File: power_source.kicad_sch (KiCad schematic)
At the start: 19 parts, among them J2 USB_B_Micro, Q1 Q_PMOS_GDS, Q2 BSS138, SW2 SW_SPDT

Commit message: make board
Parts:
- removed BT1: BackupBatt, symbol Device:Battery_Cell
- removed C5, C6: C, symbol Device:C
- removed D1: D_Schottky, symbol Device:D_Schottky
- removed D2: D, symbol Device:D
- removed J2: USB_B_Micro, symbol Connector:USB_B_Micro
- removed L1: L, symbol Device:L
- removed Q1: Q_PMOS_GDS, symbol Device:Q_PMOS_GDS
- removed Q2: BSS138, Package_TO_SOT_SMD:SOT-23, symbol Transistor_FET:BSS138
- removed R24: 10k, symbol Device:R
- removed R25: 100k, symbol Device:R
- removed R26, R27: R, symbol Device:R
- removed U7: ~, symbol balloon_lib:NJW1616F1-AT
- added C17 (x2): 4.7u, Capacitor_SMD:C_0603_1608Metric_Pad1.08x0.95mm_HandSolder, symbol Device:C
- added C4 (x3): 100n, Capacitor_SMD:C_0603_1608Metric_Pad1.08x0.95mm_HandSolder, symbol Device:C
- added D3, D4: OSG50603C1E, LED_SMD:LED_0603_1608Metric_Pad1.05x0.95mm_HandSolder, symbol Device:LED
- added D5: RS1M, Diode_SMD:D_SMA_Handsoldering, symbol Device:D
- added Q1, Q3: BSS138, Package_TO_SOT_SMD:SOT-23, symbol Transistor_FET:BSS138
- added Q2: 2SJ681, Package_TO_SOT_THT:SIPAK_Vertical, symbol Device:Q_PMOS_GDS
- added R29: 100, Resistor_SMD:R_0603_1608Metric_Pad0.98x0.95mm_HandSolder, symbol Device:R
- added R30: 10k, Resistor_SMD:R_0603_1608Metric_Pad0.98x0.95mm_HandSolder, symbol Device:R
- added R31, R32: 2.2k, Resistor_SMD:R_0603_1608Metric_Pad0.98x0.95mm_HandSolder, symbol Device:R
- added U10, U9: TCK107AF, Package_TO_SOT_SMD:SOT-23-5_HandSoldering, symbol balloon_lib:TCK107
- added U7: M78AR033-1, Package_TO_SOT_THT:TO-220-3_Vertical, symbol Regulator_Linear:LM7805_TO220
- added U8: MCP3425A0T-ECH, Package_TO_SOT_SMD:SOT-23-6_Handsoldering, symbol Analog_ADC:MCP3425A0T-ECH
- BT2, BT3, BT4: footprint (none) -> balloon:CR123A
- R28: footprint (none) -> Resistor_SMD:R_0603_1608Metric_Pad0.98x0.95mm_HandSolder
- SW2: footprint (none) -> Connector_PinSocket_2.54mm:PinSocket_1x03_P2.54mm_Vertical
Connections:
- net +3V3: now also C17.1, C17.1, C4.1, C4.1, C4.1, U10.5 (VIN), U7.3 (VO), U8.5 (Vdd), U9.5 (VIN)
- net GND1: now also C17.2, C17.2, C4.2, C4.2, C4.2, Q1.2 (S), Q3.2 (S), R31.2, R32.2, U10.2 (GND), U7.2 (GND), U8.2 (Vss), U8.6 (Vin-), U9.2 (GND)
- net at R28.1: now also BT2.1 (+), Q2.3 (S), R30.1; no longer SW2.3 (C)
- net at R28.2: now also Q1.3 (D), Q3.1 (G)
- net at SW2.2 (B): now also D3.2 (A), D5.1 (K), Q2.2 (D)
- new net: D4.1 (K), R32.1
- new net: Q2.1 (G), Q3.3 (D), R30.2
- new net: D3.1 (K), R31.1
- new net: Q1.1 (G), R29.2
- new net 5VIN: D4.2 (A), D5.2 (A), R29.1
- new net CTRL_COMM: U10.3 (CTRL)
- new net CTRL_SENSE: U9.3 (CTRL)
- new net SCL: U8.3 (SCL)
- new net SDA: U8.4 (SDA)
- new net VCOMM: U10.1 (VOUT)
- new net VIN: SW2.3 (C), U7.1 (VI), U8.1 (Vin+)
- new net VSENSE: U9.1 (VOUT)
- no-connect marks 4 -> 1
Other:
- moved on the sheet: BT2, BT3, BT4

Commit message: replace PCB
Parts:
- added J8: Bypass, Connector_PinSocket_2.54mm:PinSocket_1x02_P2.54mm_Vertical, symbol Connector:Conn_01x02_Pin
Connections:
- net GND1: now also J8.2 (Pin_2)
- net at BT3.2 (-), BT4.1 (+): now also J8.1 (Pin_1)
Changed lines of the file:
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@@
   (junction (at 151.13 76.2) (diameter 0) (color 0 0 0 0)
   )
+  (junction (at 58.42 107.95) (diameter 0) (color 0 0 0 0)
+  )
   (junction (at 176.53 83.82) (diameter 0) (color 0 0 0 0)
+  )
+  (junction (at 58.42 100.33) (diameter 0) (color 0 0 0 0)
   )
   (junction (at 73.66 80.01) (diameter 0) (color 0 0 0 0)
@@
     (stroke (width 0) (type default))
   )
+  (wire (pts (xy 44.45 104.14) (xy 49.53 104.14))
+    (stroke (width 0) (type default))
+  )
   (wire (pts (xy 165.1 134.62) (xy 171.45 134.62))
     (stroke (width 0) (type default))
@@
     (stroke (width 0) (type default))
   )
+  (wire (pts (xy 44.45 106.68) (xy 44.45 107.95))
+    (stroke (width 0) (type default))
+  )
   (wire (pts (xy 71.12 111.76) (xy 71.12 128.27))
     (stroke (width 0) (type default))
@@
     (stroke (width 0) (type default))
   )
+  (wire (pts (xy 44.45 107.95) (xy 58.42 107.95))
+    (stroke (width 0) (type default))
+  )
   (wire (pts (xy 93.98 87.63) (xy 99.06 87.63))
     (stroke (width 0) (type default))
@@
     (stroke (width 0) (type default))
   )
+  (wire (pts (xy 49.53 104.14) (xy 49.53 100.33))
+    (stroke (width 0) (type default))
+  )
   (wire (pts (xy 62.23 80.01) (xy 58.42 80.01))
+    (stroke (width 0) (type default))
+  )
+  (wire (pts (xy 49.53 100.33) (xy 58.42 100.33))
     (stroke (width 0) (type default))
   )
@@
         )
       )
+    )
+  )
+  (symbol (lib_id "Connector:Conn_01x02_Pin") (at 39.37 104.14 0) (unit 1)
+    (in_bom yes) (on_board yes) (dnp no) (fields_autoplaced)
+    (property "Reference" "J8" (at 40.005 99.9195 0)
+      (effects (font (size 1.27 1.27)))
+    )
+    (property "Value" "Bypass" (at 40.005 102.3437 0)
+      (effects (font (size 1.27 1.27)))
+    )
+    (property "Footprint" "Connector_PinSocket_2.54mm:PinSocket_1x02_P2.54mm_Vertical" (at 39.37 104.14 0)
+      (effects (font (size 1.27 1.27)) hide)
+    )
+    (property "Datasheet" "~" (at 39.37 104.14 0)
+      (effects (font (size 1.27 1.27)) hide)
+    )
+    (pin "2")
+    (pin "1")
+    (instances
+      (project "balloon"
+        (path "/390c33b5-3f3b-4c86-a202-e8d785058178/a8964fff-36f8-4d65-a455-a6f79e0406e2"
+          (reference "J8") (unit 1)
+        )
+      )

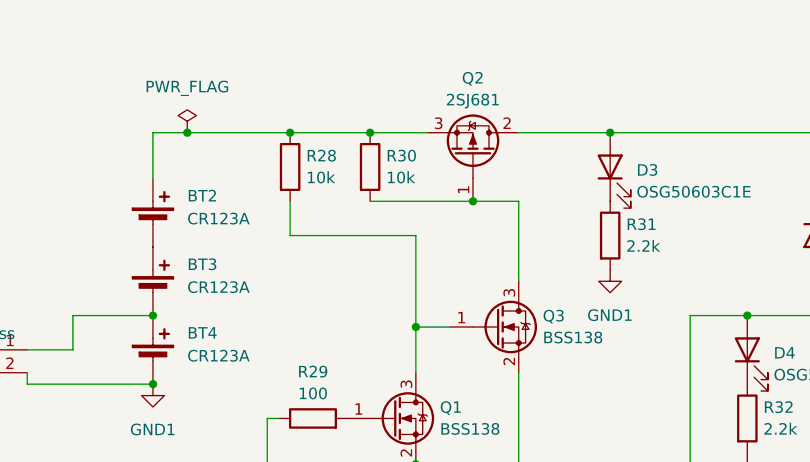
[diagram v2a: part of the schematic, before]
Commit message: add stmcube
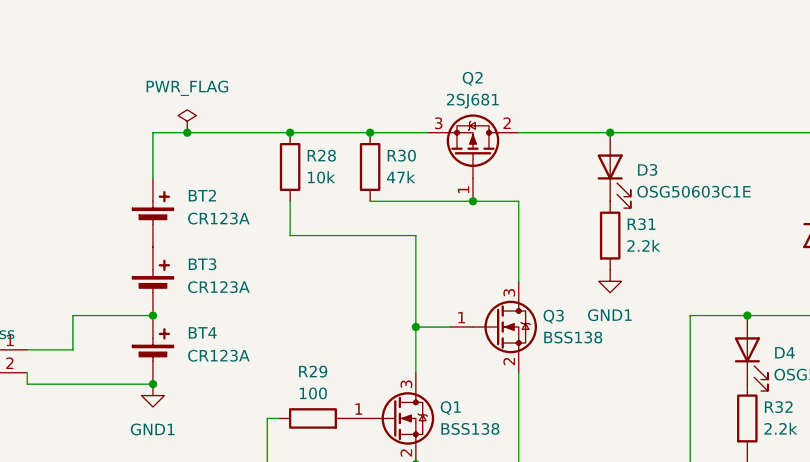
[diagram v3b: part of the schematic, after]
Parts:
- R30: value 10k -> 47k
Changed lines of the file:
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@@
       (effects (font (size 1.27 1.27)) hide)
     )
-    (pin "2")
-    (pin "1")
+    (pin "1")
+    (pin "2")
     (instances
       (project "balloon"
@@
       (effects (font (size 1.27 1.27)) hide)
     )
+    (pin "1")
+    (pin "2")
+    (pin "3")
+    (pin "4")
     (pin "5")
-    (pin "4")
-    (pin "1")
-    (pin "3")
-    (pin "2")
     (pin "6")
     (instances
@@
       (effects (font (size 1.27 1.27)) hide)
     )
-    (pin "2")
-    (pin "1")
+    (pin "1")
+    (pin "2")
     (pin "3")
     (instances
@@
       (effects (font (size 1.27 1.27)) hide)
     )
-    (pin "2")
-    (pin "1")
+    (pin "1")
+    (pin "2")
     (instances
       (project "balloon"
@@
       (effects (font (size 1.27 1.27)) hide)
     )
+    (pin "1")
     (pin "2")
     (pin "3")
-    (pin "1")
+    (pin "4")
     (pin "5")
-    (pin "4")
     (instances
       (project "balloon"
@@
       (effects (font (size 1.27 1.27)) hide)
     )
+    (pin "1")
+    (pin "2")
     (pin "3")
-    (pin "2")
-    (pin "1")
     (instances
       (project "balloon"
@@
       (effects (font (size 1.27 1.27)) (justify left))
     )
-    (property "Value" "10k" (at 84.328 85.0321 0)
+    (property "Value" "47k" (at 84.328 85.0321 0)
       (effects (font (size 1.27 1.27)) (justify left))
     )
@@
       (effects (font (size 1.27 1.27)) hide)
     )
+    (pin "1")
     (pin "2")
     (pin "3")
-    (pin "1")
+    (pin "4")
     (pin "5")
-    (pin "4")
-    (instances
-      (project "balloon"
+    (instances
+      (project "balloon"

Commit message: set gerber
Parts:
- U10, U9: Price (none) -> 30
- U7: Price (none) -> 500
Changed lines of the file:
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@@
+      (effects (font (size 1.27 1.27)) hide)
+    )
+    (property "Price" "" (at 124.46 111.76 0)
       (effects (font (size 1.27 1.27)) hide)
     )
@@
       (effects (font (size 1.27 1.27)) hide)
     )
+    (property "Price" "" (at 190.5 80.01 0)
+      (effects (font (size 1.27 1.27)) hide)
+    )
     (pin "1")
     (pin "2")
@@
       (effects (font (size 1.27 1.27)) (justify left) hide)
     )
+    (property "Price" "" (at 96.52 101.6 0)
+      (effects (font (size 1.27 1.27)) hide)
+    )
     (pin "1")
     (pin "2")
@@
     )
     (property "Datasheet" "~" (at 109.22 91.44 0)
+      (effects (font (size 1.27 1.27)) hide)
+    )
+    (property "Price" "" (at 109.22 91.44 0)
       (effects (font (size 1.27 1.27)) hide)
     )
@@
       (effects (font (size 1.27 1.27)) hide)
     )
+    (property "Price" "" (at 219.71 107.95 0)
+      (effects (font (size 1.27 1.27)) hide)
+    )
     (pin "1")
     (pin "2")
@@
       (effects (font (size 1.27 1.27)) hide)
     )
+    (property "Price" "" (at 73.66 83.82 0)
+      (effects (font (size 1.27 1.27)) hide)
+    )
     (pin "1")
     (pin "2")
@@
     )
     (property "Datasheet" "~" (at 58.42 103.886 90)
+      (effects (font (size 1.27 1.27)) hide)
+    )
+    (property "Price" "" (at 58.42 105.41 0)
       (effects (font (size 1.27 1.27)) hide)
     )
@@
       (effects (font (size 1.27 1.27)) hide)
     )
+    (property "Price" "" (at 201.93 80.01 0)
+      (effects (font (size 1.27 1.27)) hide)
+    )
     (pin "1")
     (pin "2")
@@
     )
     (property "Datasheet" "http://ww1.microchip.com/downloads/en/DeviceDoc/22072b.pdf" (at 184.15 132.08 0)
+      (effects (font (size 1.27 1.27)) hide)
+    )
+    (property "Price" "" (at 184.15 132.08 0)
       (effects (font (size 1.27 1.27)) hide)
     )
@@
       (effects (font (size 1.27 1.27)) hide)
     )
+    (property "Price" "" (at 109.22 83.82 0)
+      (effects (font (size 1.27 1.27)) hide)
+    )
     (pin "1")
     (pin "2")
@@
       (effects (font (size 1.27 1.27)) hide)
     )
+    (property "Price" "500" (at 176.53 76.2 0)
+      (effects (font (size 1.27 1.27)) hide)
+    )
     (pin "1")
     (pin "2")
@@
       (effects (font (size 1.27 1.27)) hide)
     )
+    (property "Price" "" (at 58.42 90.17 0)
+      (effects (font (size 1.27 1.27)) hide)
+    )
     (pin "1")
     (pin "2")
@@
       (effects (font (size 1.27 1.27)) hide)
     )
+    (property "Price" "" (at 39.37 104.14 0)
+      (effects (font (size 1.27 1.27)) hide)
+    )
     (pin "1")
     (pin "2")
@@
       (effects (font (size 1.27 1.27)) hide)
     )
+    (property "Price" "" (at 199.39 144.78 0)
+      (effects (font (size 1.27 1.27)) hide)
+    )
     (pin "1")
     (pin "2")
@@
     )
     (property "Datasheet" "~" (at 76.2 111.76 0)
+      (effects (font (size 1.27 1.27)) hide)
+    )
+    (property "Price" "" (at 76.2 111.76 0)
       (effects (font (size 1.27 1.27)) hide)
     )
@@
       (effects (font (size 1.27 1.27)) hide)
     )
+    (property "Price" "30" (at 250.19 125.73 0)
+      (effects (font (size 1.27 1.27)) hide)
+    )
     (pin "1")
     (pin "2")
@@
       (effects (font (size 1.27 1.27)) hide)
     )
+    (property "Price" "" (at 132.08 91.44 0)
+      (effects (font (size 1.27 1.27)) hide)
+    )
     (pin "1")
     (pin "2")
@@
       (effects (font (size 1.27 1.27)) hide)
     )
+    (property "Price" "" (at 124.46 104.14 0)
+      (effects (font (size 1.27 1.27)) hide)
+    )
     (pin "1")
     (pin "2")
@@
     )
     (property "Datasheet" "~" (at 58.42 96.266 90)
+      (effects (font (size 1.27 1.27)) hide)
+    )
+    (property "Price" "" (at 58.42 97.79 0)
       (effects (font (size 1.27 1.27)) hide)
     )
@@
       (effects (font (size 1.27 1.27)) hide)
     )
+    (property "Price" "" (at 93.98 82.55 0)
+      (effects (font (size 1.27 1.27)) hide)
+    )
     (pin "1")
     (pin "2")
@@
     (property "Datasheet" "https://www.onsemi.com/pub/Collateral/BSS138-D.PDF" (at 85.09 111.76 0)
       (effects (font (size 1.27 1.27)) (justify left) hide)
+    )
+    (property "Price" "" (at 85.09 111.76 0)
+      (effects (font (size 1.27 1.27)) hide)
     )
     (pin "1")
@@
       (effects (font (size 1.27 1.27)) hide)
     )
+    (property "Price" "" (at 219.71 128.27 0)
+      (effects (font (size 1.27 1.27)) hide)
+    )
     (pin "1")
     (pin "2")
@@
     )
     (property "Datasheet" "~" (at 82.55 83.82 0)
+      (effects (font (size 1.27 1.27)) hide)
+    )
+    (property "Price" "" (at 82.55 83.82 0)
       (effects (font (size 1.27 1.27)) hide)
     )
@@
       (effects (font (size 1.27 1.27)) hide)
     )
+    (property "Price" "30" (at 250.19 109.22 0)
+      (effects (font (size 1.27 1.27)) hide)
+    )
     (pin "1")
     (pin "2")
@@
       (effects (font (size 1.27 1.27)) hide)
     )
+    (property "Price" "" (at 139.7 76.2 0)
+      (effects (font (size 1.27 1.27)) hide)
+    )

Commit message: change pow
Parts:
- removed D3, D4: OSG50603C1E, LED_SMD:LED_0603_1608Metric_Pad1.05x0.95mm_HandSolder, symbol Device:LED
- removed D5: RS1M, Diode_SMD:D_SMA_Handsoldering, symbol Device:D
- removed Q1, Q3: BSS138, Package_TO_SOT_SMD:SOT-23, symbol Transistor_FET:BSS138
- removed Q2: 2SJ681, Package_TO_SOT_THT:SIPAK_Vertical, symbol Device:Q_PMOS_GDS
- added Q1, Q2: Si9933ADY, symbol Device:Q_Dual_PMOS_S1G1S2G2D2D2D1D1
- added R37, R38, R39, R40, R41, R42: R, symbol Device:R
- added SW3: SW_SPDT, Connector_PinSocket_2.54mm:PinSocket_1x03_P2.54mm_Vertical, symbol Switch:SW_SPDT
- added U2: LTC4417CGN, Package_SO:SSOP-24_3.9x8.7mm_P0.635mm, symbol Power_Management:LTC4417CGN
- R28: value 10k -> R; footprint Resistor_SMD:R_0603_1608Metric_Pad0.98x0.95mm_HandSolder -> (none)
- R29: value 100 -> R; footprint Resistor_SMD:R_0603_1608Metric_Pad0.98x0.95mm_HandSolder -> (none)
- R30: value 47k -> R; footprint Resistor_SMD:R_0603_1608Metric_Pad0.98x0.95mm_HandSolder -> (none)
- R31, R32: value 2.2k -> R; footprint Resistor_SMD:R_0603_1608Metric_Pad0.98x0.95mm_HandSolder -> (none)
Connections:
- net +3V3: now also SW2.1 (A); no longer U7.3 (VO)
- net 5VIN: now also R31.1, Q2.7 (D), Q2.8 (G), R41.1, U2.24 (V1); no longer R29.1
- net GND1: now also R30.2, R37.2, R40.2, SW3.3 (C), U2.13 (GND), U2.3 (HYS); no longer R31.2, R32.2
- net VIN: now also Q1.5 (D), Q1.6 (G), Q2.5 (D), Q2.6 (G); no longer SW2.3 (C)
- net at R32.1: now also R31.2, U2.4 (UV1)
- net at R28.2: now also R29.1, U2.6 (UV2)
- net at BT2.1 (+), R28.1: now also Q1.7 (D), Q1.8 (G), R42.1, U2.23 (V2); no longer R30.1
- net at SW2.2 (B): now also U7.3 (VO), R38.1, U2.22 (V3)
- net at R29.2: now also R30.1, U2.7 (OV2)
- new net: Q1.1 (S), Q1.3 (S), U2.19 (VS2)
- new net: Q1.2 (G), Q1.4 (G), U2.18 (G2)
- new net: R32.2, R37.1, U2.5 (OV1)
- new net: Q2.1 (S), Q2.3 (S), U2.21 (VS1)
- new net: Q2.2 (G), Q2.4 (G), U2.20 (G1)
- new net: R39.2, R40.1, U2.9 (OV3)
- new net: R41.2, R42.2, SW3.2 (B), U2.1 (EN)
- new net: R38.2, R39.1, U2.8 (UV3)
- no-connect marks 1 -> 2
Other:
- moved on the sheet: BT2, BT3, BT4, C17, C4, J8, U10, U7, U8, U9

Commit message: add communication
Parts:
- removed Q1, Q2: Si9933ADY, symbol Device:Q_Dual_PMOS_S1G1S2G2D2D2D1D1
- removed R28, R29, R30, R31, R32, R37, R38, R39, R40, R41, R42: R, symbol Device:R
- removed SW3: SW_SPDT, Connector_PinSocket_2.54mm:PinSocket_1x03_P2.54mm_Vertical, symbol Switch:SW_SPDT
- removed U2: LTC4417CGN, Package_SO:SSOP-24_3.9x8.7mm_P0.635mm, symbol Power_Management:LTC4417CGN
- added D3: D, symbol Device:D
- added Q1: Q_PMOS_GDS, symbol Device:Q_PMOS_GDS
- renumbered BT2 to BT1, BT3 to BT2, BT4 to BT3, C4 to C15, C4 to C16, C17 to C18, C4 to C19, C17 to C20
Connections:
- net VIN: now also D3.1 (K), Q1.3 (S)
- net at BT1.1 (+): now also Q1.2 (D)
- new net 12VDC: D3.2 (A), Q1.1 (G)
- no-connect marks 2 -> 1
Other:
- moved on the sheet: BT1, BT2, BT3, J8
